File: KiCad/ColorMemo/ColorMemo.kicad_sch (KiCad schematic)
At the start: 49 parts, among them SW1 SW_Push, SW10 SW_Push, SW11 SW_Push, SW12 SW_Push, SW13 SW_Push, SW14 SW_Push, SW15 SW_Push, SW16 SW_Push, SW17 SW_Push, SW18 SW_Push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

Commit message: added kicad project
Signed-off-by: Michal Pelka <michalpelka@gmail.com>
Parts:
- SW1, SW10, SW11, SW12, SW13, SW14, SW15, SW16, SW17, SW18, SW19, SW2, SW20, SW21, SW22, SW23, SW24, SW3, SW4, SW5, SW6, SW7, SW8, SW9: footprint Button_Switch_THT:SW_PUSH-12mm -> Button_Switch_THT:SW_PUSH_6mm
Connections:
- net GND: now also D10.3 (VSS), D2.3 (VSS), D6.3 (VSS); no longer D10.1 (VDD), D2.1 (VDD), D6.1 (VDD)
- net MUL_ROW_1: no longer SW17.2, SW18.2, SW19.2, SW20.2, SW21.2, SW22.2, SW23.2, SW24.2
- net MUL_ROW_2: now also SW17.2, SW18.2, SW19.2, SW20.2, SW21.2, SW22.2, SW23.2, SW24.2
- net VCC: now also D10.1 (VDD), D2.1 (VDD), D6.1 (VDD); no longer D10.3 (VSS), D2.3 (VSS), D6.3 (VSS)
- net at D3.4 (DIN): now also D2.2 (DOUT); no longer D2.4 (DIN)
- net at D10.2 (DOUT): now also D11.4 (DIN); no longer D9.2 (DOUT)
- net at D10.4 (DIN): now also D9.2 (DOUT); no longer D11.4 (DIN)
- net at D6.2 (DOUT): now also D7.4 (DIN); no longer D5.2 (DOUT)
- net at D6.4 (DIN): now also D5.2 (DOUT); no longer D7.4 (DIN)
- net at D1.2 (DOUT): now also D2.4 (DIN); no longer D2.2 (DOUT)
- net at D8.2 (DOUT): now also D9.4 (DIN)
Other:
- moved on the sheet: D10, D2, D6

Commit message: order to jlcpcb
Signed-off-by: Michal Pelka <michalpelka@gmail.com>
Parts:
- added BZ1: Buzzer, Buzzer_Beeper:Buzzer_12x9.5RM7.6, symbol Device:Buzzer
- added C13: C_Polarized, Capacitor_THT:CP_Radial_D8.0mm_P5.00mm, symbol Device:C_Polarized
- added D13: 1N4148WT, Diode_SMD:D_SOD-523, symbol Diode:1N4148WT
- added H1, H2, H3, H4, H5, H6, H7: MountingHole, MountingHole:MountingHole_3.2mm_M3, symbol Mechanical:MountingHole
- added J1: Conn_01x02, Connector_JST:JST_PH_B2B-PH-K_1x02_P2.00mm_Vertical, symbol Connector_Generic:Conn_01x02
- added Q1: MMFTN3402, Package_TO_SOT_SMD:SOT-23, symbol Transistor_FET:Q_NMOS_GSD
- added R1: R100, Resistor_SMD:R_0805_2012Metric_Pad1.20x1.40mm_HandSolder, symbol Device:R_Small
- added R2: 100k, Resistor_SMD:R_0805_2012Metric_Pad1.20x1.40mm_HandSolder, symbol Device:R_Small
- added R3: R330, Resistor_SMD:R_0805_2012Metric_Pad1.20x1.40mm_HandSolder, symbol Device:R_Small
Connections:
- net GND: now also C13.2, D13.2 (A), J1.2 (Pin_2), Q1.2 (S), R2.2
- net VCC: now also BZ1.1 (+), C13.1, D13.1 (K), J1.1 (Pin_1)
- net at U1.13 (SDA/D2): now also R1.2
- net at U1.14 (SCL/D1): now also R3.1; no longer D1.4 (DIN)
- new net: Q1.1 (G), R1.1, R2.1
- new net: D1.4 (DIN), R3.2
- new net: BZ1.2 (-), Q1.3 (D)

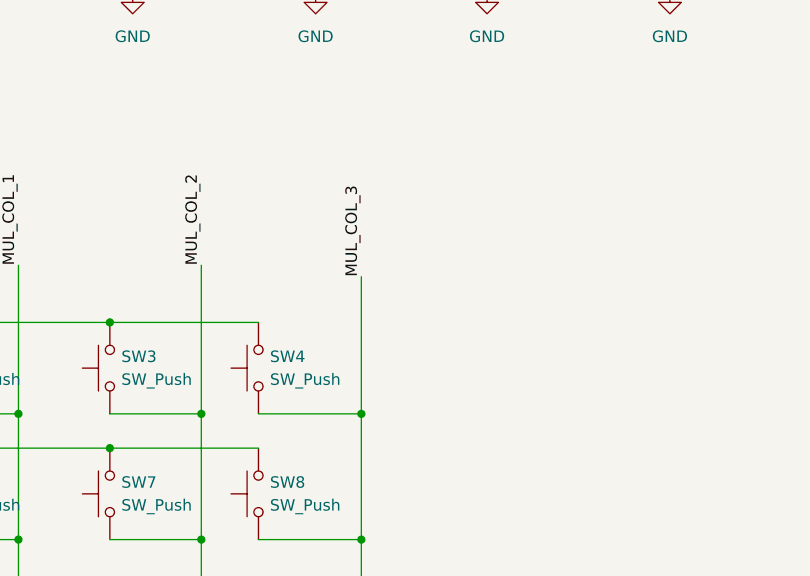
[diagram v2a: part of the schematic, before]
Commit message: Added readme, CAD
Signed-off-by: Michal Pelka <michalpelka@gmail.com>
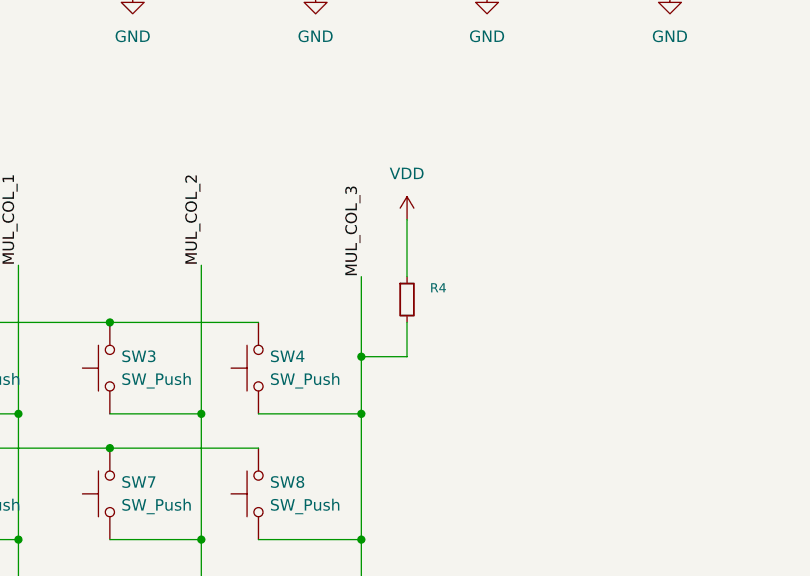
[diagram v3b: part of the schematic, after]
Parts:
- added R4: 10k, Resistor_SMD:R_0805_2012Metric_Pad1.20x1.40mm_HandSolder, symbol Device:R_Small
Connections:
- net MUL_COL_3: now also R4.2
- net VDD: now also R4.1
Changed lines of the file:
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@@
 	)
 	(junction
+		(at 152.4 129.54)
+		(diameter 0)
+		(color 0 0 0 0)
+	)
+	(junction
 		(at 105.41 200.66)
 		(diameter 0)
@@
 	(wire
 		(pts
-			(xy 152.4 120.65) (xy 152.4 135.89)
+			(xy 152.4 120.65) (xy 152.4 129.54)
 		)
 		(stroke
@@
 	(wire
 		(pts
+			(xy 157.48 129.54) (xy 152.4 129.54)
+		)
+		(stroke
+			(width 0)
+			(type default)
+		)
+	)
+	(wire
+		(pts
 			(xy 124.46 186.69) (xy 140.97 186.69)
 		)
@@
 	(wire
 		(pts
+			(xy 157.48 125.73) (xy 157.48 129.54)
+		)
+		(stroke
+			(width 0)
+			(type default)
+		)
+	)
+	(wire
+		(pts
 			(xy 304.8 60.96) (xy 304.8 63.5)
 		)
@@
 	(wire
 		(pts
+			(xy 157.48 114.3) (xy 157.48 120.65)
+		)
+		(stroke
+			(width 0)
+			(type default)
+		)
+	)
+	(wire
+		(pts
 			(xy 140.97 210.82) (xy 152.4 210.82)
 		)
@@
 	(wire
 		(pts
+			(xy 152.4 129.54) (xy 152.4 135.89)
+		)
+		(stroke
+			(width 0)
+			(type default)
+		)
+	)
+	(wire
+		(pts
 			(xy 292.1 53.34) (xy 297.18 53.34)
 		)
@@
 	)
 	(symbol
+		(lib_id "power:VDD")
+		(at 157.48 114.3 0)
+		(unit 1)
+		(exclude_from_sim no)
+		(in_bom yes)
+		(on_board yes)
+		(dnp no)
+		(fields_autoplaced yes)
+		(property "Reference" "#PWR057"
+			(at 157.48 118.11 0)
+			(effects
+				(font
+					(size 1.27 1.27)
+				)
+				(hide yes)
+			)
+		)
+		(property "Value" "VDD"
+			(at 157.48 109.22 0)
+			(effects
+				(font
+					(size 1.27 1.27)
+				)
+			)
+		)
+		(property "Footprint" ""
+			(at 157.48 114.3 0)
+			(effects
+				(font
+					(size 1.27 1.27)
+				)
+				(hide yes)
+			)
+		)
+		(property "Datasheet" ""
+			(at 157.48 114.3 0)
+			(effects
+				(font
+					(size 1.27 1.27)
+				)
+				(hide yes)
+			)
+		)
+		(property "Description" "Power symbol creates a global label with name \"VDD\""
+			(at 157.48 114.3 0)
+			(effects
+				(font
+					(size 1.27 1.27)
+				)
+				(hide yes)
+			)
+		)
+		(pin "1"
+		)
+		(instances
+			(project ""
+				(path "/91f2b27b-9d5b-4758-ab43-71d69bcbd8a1"
+					(reference "#PWR057")
+					(unit 1)
+				)
+			)
+		)
+	)
+	(symbol
 		(lib_id "power:VCC")
 		(at 264.16 76.2 0)
@@
 					(unit 1)
 				)
+			)
+		)
+	)
+	(symbol
+		(lib_id "Device:R_Small")
+		(at 157.48 123.19 0)
+		(unit 1)
+		(exclude_from_sim no)
+		(in_bom yes)
+		(on_board yes)
+		(dnp no)
+		(fields_autoplaced yes)
+		(property "Reference" "R4"
+			(at 160.02 121.9199 0)
+			(effects
+				(font
+					(size 1.016 1.016)
+				)
+				(justify left)
+			)
+		)
+		(property "Value" "10k"
+			(at 160.02 124.4599 0)
+			(effects
+				(font
+					(size 1.27 1.27)
+				)
+				(justify left)
+				(hide yes)
+			)
+		)
+		(property "Footprint" "Resistor_SMD:R_0805_2012Metric_Pad1.20x1.40mm_HandSolder"
+			(at 157.48 123.19 0)
+			(effects
+				(font
+					(size 1.27 1.27)
+				)
+				(hide yes)
+			)
+		)
+		(property "Datasheet" "~"
+			(at 157.48 123.19 0)
+			(effects
+				(font
+					(size 1.27 1.27)
+				)
+				(hide yes)
+			)
+		)
+		(property "Description" "Resistor, small symbol"
+			(at 157.48 123.19 0)
+			(effects
+				(font
+					(size 1.27 1.27)
+				)
+				(hide yes)
+			)
+		)
+		(pin "1"
+		)
+		(pin "2"
+		)
+		(instances
+			(project "ColorMemo"
+				(path "/91f2b27b-9d5b-4758-ab43-71d69bcbd8a1"
+					(reference "R4")
+					(unit 1)
+				)
